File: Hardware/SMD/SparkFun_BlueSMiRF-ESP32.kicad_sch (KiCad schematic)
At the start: 27 parts, among them J1 Conn_01x06, Q1 Q_NMOS_DGS, Q2 Q_NMOS_DGS, SW1 Switch, U1 ESP32_Pico_Mini, U2 AP2112K-3.3

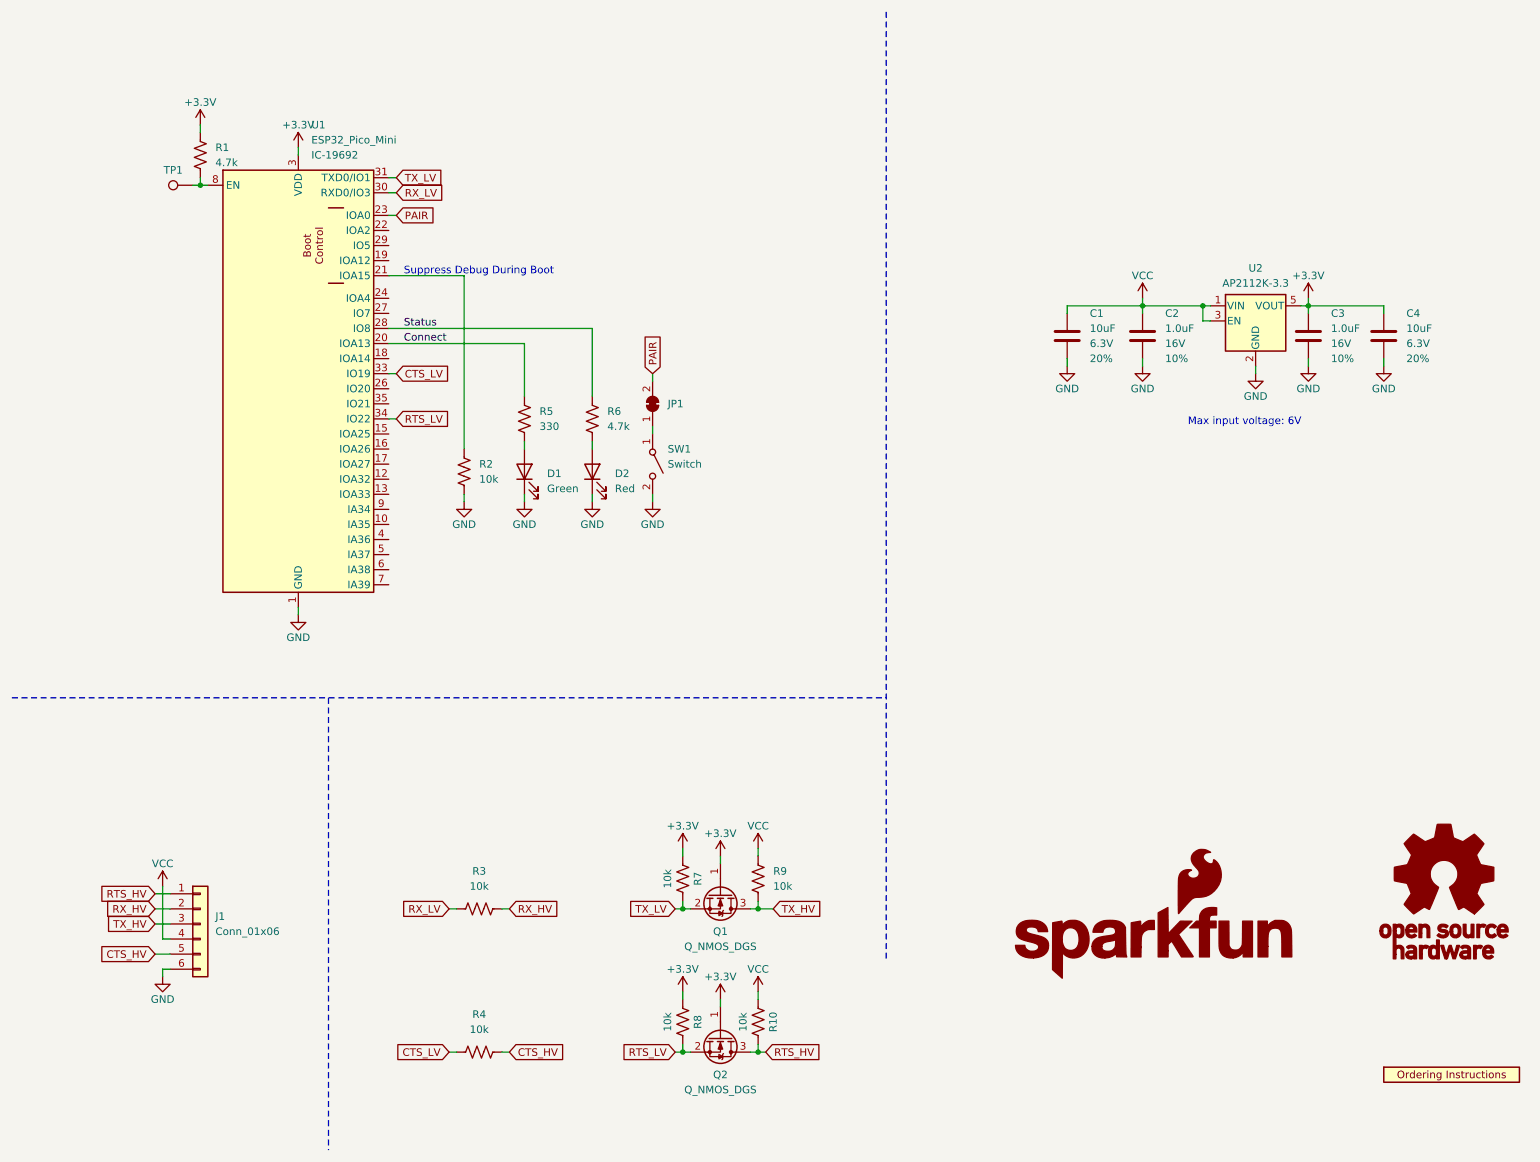
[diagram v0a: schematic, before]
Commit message: Post design review fixes.
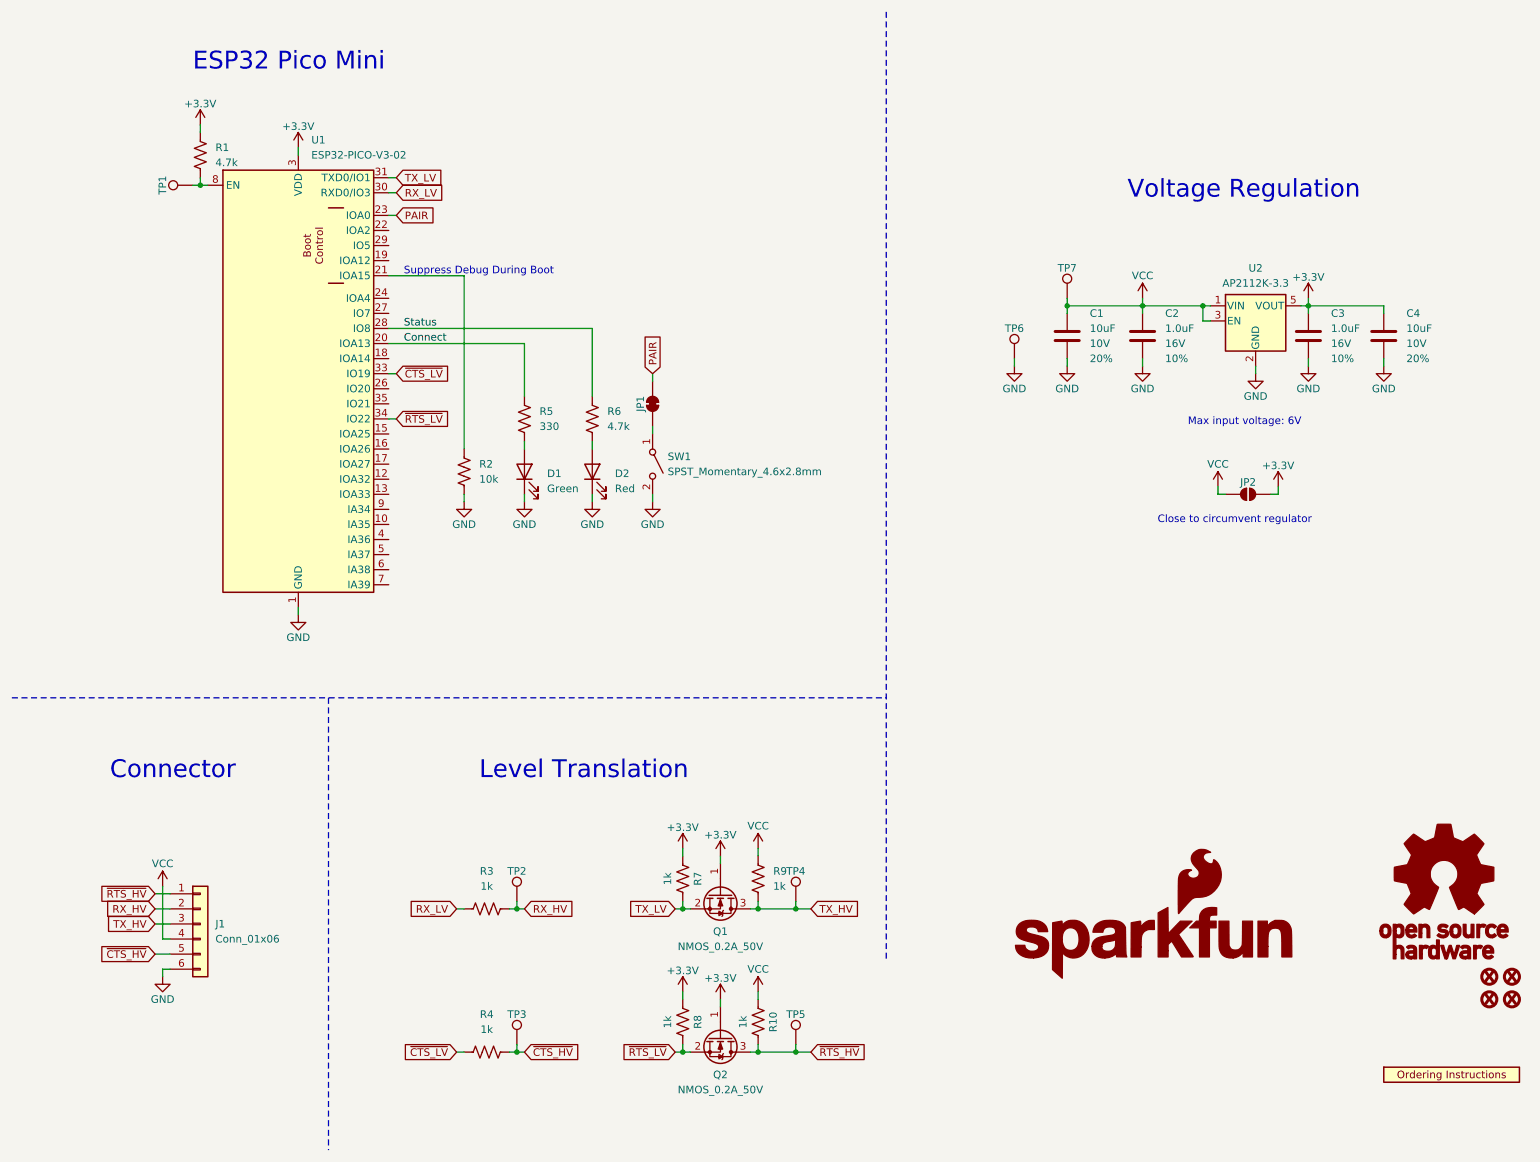
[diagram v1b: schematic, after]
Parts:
- added FID1, FID2, FID3, FID4: Fiducial_0.5, SparkFun-Aesthetic:Fiducial_0.5mm_Mask1mm, symbol SparkFun-Aesthetic:Fiducial_0.5
- added JP2: ~, SparkFun-Jumper:SMT-JUMPER_2_NO_SILK, symbol SparkFun-Jumper:SolderJumper_2_Open
- added TP2, TP3, TP4, TP5, TP6, TP7: TestPoint_0.75mm, SparkFun-Connector:TestPoint-0.75mm, symbol SparkFun-Connector:TestPoint_0.75mm
- C1, C4: symbol SparkFun-Capacitor:10uF_0603_6.3V_20% -> SparkFun-Capacitor:10uF_0603_10V_20%; PROD_ID CAP-11015 -> CAP-20155; Voltage 6.3V -> 10V
- Q1, Q2: value Q_NMOS_DGS -> NMOS_0.2A_50V
- R10, R3, R4, R7, R8, R9: value 10k -> 1k; symbol SparkFun-Resistor:10k_0603 -> SparkFun-Resistor:1k_0603; PROD_ID RES-00824 -> RES-07856
- SW1: value Switch -> SPST_Momentary_4.6x2.8mm
- U1: value ESP32_Pico_Mini -> ESP32-PICO-V3-02
- U3: footprint SparkFun-Aesthetic:Ordering_Instructions -> SparkFun-Aesthetic:ORDERING_INSTRUCTIONS
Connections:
- net +3.3V: now also JP2.2 (B)
- net GND: now also TP6.1
- net RX_HV: now also TP2.1
- net TX_HV: now also TP4.1
- net VCC: now also JP2.1 (A), TP7.1
- net CTS_HV renamed ~{CTS_HV}
- net ~{CTS_HV}: now also TP3.1
- net CTS_LV renamed ~{CTS_LV}
- net RTS_HV renamed ~{RTS_HV}
- net ~{RTS_HV}: now also TP5.1
- net RTS_LV renamed ~{RTS_LV}
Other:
- note added: "Close to circumvent regulator"
- note added: "Connector"
- note added: "ESP32 Pico Mini"
- note added: "Level Translation"
- note added: "Voltage Regulation"
- title: BlueSMiRF - ESP32 -> SparkFun BlueSMiRF - ESP32
- moved on the sheet: R3, R4

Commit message: Change BSS138 resistors to 10k
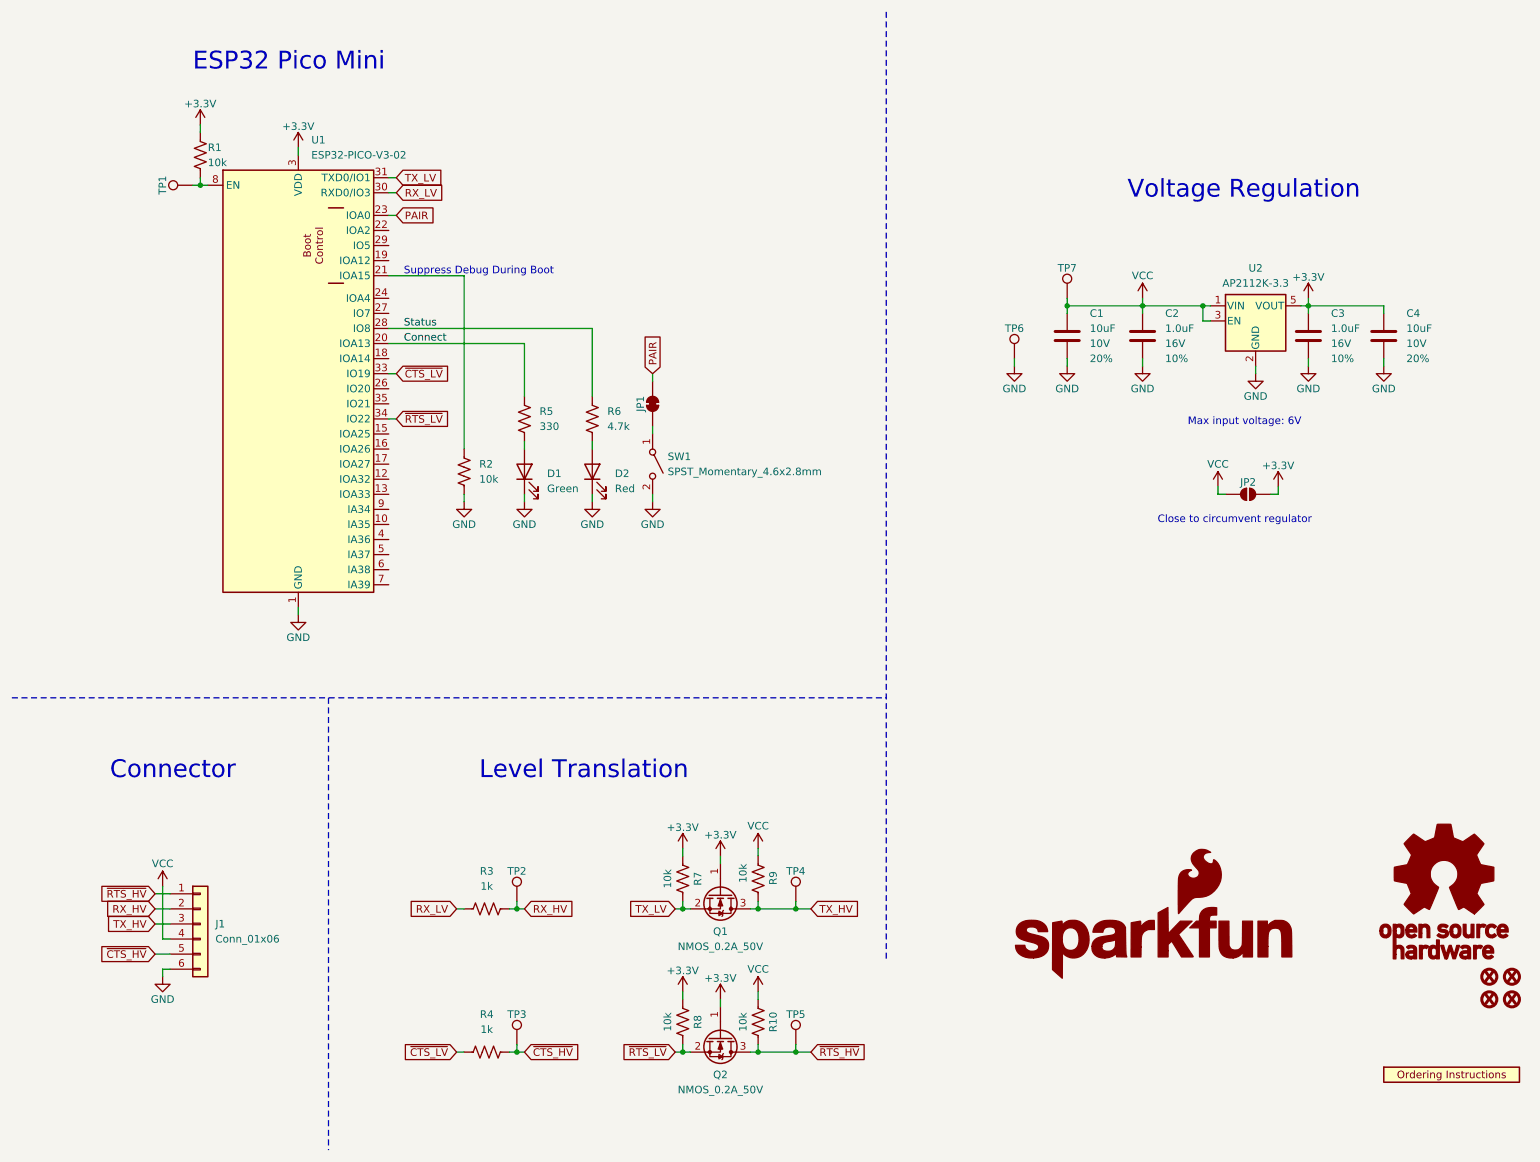
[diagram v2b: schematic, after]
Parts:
- R1: value 4.7k -> 10k; symbol SparkFun-Resistor:4.7k_0603 -> SparkFun-Resistor:10k_0603; PROD_ID RES-07857 -> RES-00824
- R10, R7, R8, R9: value 1k -> 10k; symbol SparkFun-Resistor:1k_0603 -> SparkFun-Resistor:10k_0603; PROD_ID RES-07856 -> RES-00824
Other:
- moved on the sheet: R1, R10, R7, R8, R9
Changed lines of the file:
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@@
     )
   )
-  (symbol (lib_id "SparkFun-Resistor:1k_0603") (at 125.73 157.48 0) (unit 1)
-    (in_bom yes) (on_board yes) (dnp no)
-    (property "Reference" "R7" (at 128.27 157.48 90)
-      (effects (font (size 1.27 1.27)))
-    )
-    (property "Value" "1k" (at 123.19 157.48 90)
-      (effects (font (size 1.27 1.27)))
-    )
-    (property "Footprint" "SparkFun-Resistor:R_0603_1608Metric" (at 130.302 157.48 90)
-      (effects (font (size 1.27 1.27)) hide)
-    )
-    (property "Datasheet" "https://www.vishay.com/docs/20035/dcrcwe3.pdf" (at 134.62 158.75 90)
-      (effects (font (size 1.27 1.27)) hide)
-    )
-    (property "PROD_ID" "RES-07856" (at 132.588 157.48 90)
+  (symbol (lib_name "10k_0603_1") (lib_id "SparkFun-Resistor:10k_0603") (at 125.73 157.48 90) (unit 1)
+    (in_bom yes) (on_board yes) (dnp no)
+    (property "Reference" "R7" (at 128.27 157.48 0)
+      (effects (font (size 1.27 1.27)))
+    )
+    (property "Value" "10k" (at 123.19 157.48 0)
+      (effects (font (size 1.27 1.27)))
+    )
+    (property "Footprint" "SparkFun-Resistor:R_0603_1608Metric" (at 130.048 157.48 0)
+      (effects (font (size 1.27 1.27)) hide)
+    )
+    (property "Datasheet" "https://www.vishay.com/docs/20035/dcrcwe3.pdf" (at 133.35 157.48 0)
+      (effects (font (size 1.27 1.27)) hide)
+    )
+    (property "PROD_ID" "RES-00824" (at 132.08 157.48 0)
       (effects (font (size 1.27 1.27)) hide)
     )
@@
     )
   )
-  (symbol (lib_id "SparkFun-Resistor:1k_0603") (at 138.43 157.48 0) (unit 1)
-    (in_bom yes) (on_board yes) (dnp no) (fields_autoplaced)
+  (symbol (lib_name "10k_0603_2") (lib_id "SparkFun-Resistor:10k_0603") (at 138.43 157.48 90) (unit 1)
+    (in_bom yes) (on_board yes) (dnp no)
     (property "Reference" "R9" (at 140.97 156.21 0)
-      (effects (font (size 1.27 1.27)) (justify left))
-    )
-    (property "Value" "1k" (at 140.97 158.75 0)
-      (effects (font (size 1.27 1.27)) (justify left))
-    )
-    (property "Footprint" "SparkFun-Resistor:R_0603_1608Metric" (at 143.002 157.48 90)
-      (effects (font (size 1.27 1.27)) hide)
-    )
-    (property "Datasheet" "https://www.vishay.com/docs/20035/dcrcwe3.pdf" (at 147.32 158.75 90)
-      (effects (font (size 1.27 1.27)) hide)
-    )
-    (property "PROD_ID" "RES-07856" (at 145.288 157.48 90)
+      (effects (font (size 1.27 1.27)) (justify right))
+    )
+    (property "Value" "10k" (at 135.89 154.94 0)
+      (effects (font (size 1.27 1.27)) (justify right))
+    )
+    (property "Footprint" "SparkFun-Resistor:R_0603_1608Metric" (at 142.748 157.48 0)
+      (effects (font (size 1.27 1.27)) hide)
+    )
+    (property "Datasheet" "https://www.vishay.com/docs/20035/dcrcwe3.pdf" (at 146.05 157.48 0)
+      (effects (font (size 1.27 1.27)) hide)
+    )
+    (property "PROD_ID" "RES-00824" (at 144.78 157.48 0)
       (effects (font (size 1.27 1.27)) hide)
     )
@@
     )
   )
-  (symbol (lib_id "SparkFun-Resistor:1k_0603") (at 125.73 181.61 0) (unit 1)
-    (in_bom yes) (on_board yes) (dnp no)
-    (property "Reference" "R8" (at 128.27 181.61 90)
-      (effects (font (size 1.27 1.27)))
-    )
-    (property "Value" "1k" (at 123.19 181.61 90)
-      (effects (font (size 1.27 1.27)))
-    )
-    (property "Footprint" "SparkFun-Resistor:R_0603_1608Metric" (at 130.302 181.61 90)
-      (effects (font (size 1.27 1.27)) hide)
-    )
-    (property "Datasheet" "https://www.vishay.com/docs/20035/dcrcwe3.pdf" (at 134.62 182.88 90)
-      (effects (font (size 1.27 1.27)) hide)
-    )
-    (property "PROD_ID" "RES-07856" (at 132.588 181.61 90)
+  (symbol (lib_name "10k_0603_3") (lib_id "SparkFun-Resistor:10k_0603") (at 125.73 181.61 90) (unit 1)
+    (in_bom yes) (on_board yes) (dnp no)
+    (property "Reference" "R8" (at 128.27 181.61 0)
+      (effects (font (size 1.27 1.27)))
+    )
+    (property "Value" "10k" (at 123.19 181.61 0)
+      (effects (font (size 1.27 1.27)))
+    )
+    (property "Footprint" "SparkFun-Resistor:R_0603_1608Metric" (at 130.048 181.61 0)
+      (effects (font (size 1.27 1.27)) hide)
+    )
+    (property "Datasheet" "https://www.vishay.com/docs/20035/dcrcwe3.pdf" (at 133.35 181.61 0)
+      (effects (font (size 1.27 1.27)) hide)
+    )
+    (property "PROD_ID" "RES-00824" (at 132.08 181.61 0)
       (effects (font (size 1.27 1.27)) hide)
     )
@@
     )
   )
-  (symbol (lib_id "SparkFun-Resistor:1k_0603") (at 138.43 181.61 0) (unit 1)
-    (in_bom yes) (on_board yes) (dnp no)
-    (property "Reference" "R10" (at 140.97 181.61 90)
-      (effects (font (size 1.27 1.27)))
-    )
-    (property "Value" "1k" (at 135.89 181.61 90)
-      (effects (font (size 1.27 1.27)))
-    )
-    (property "Footprint" "SparkFun-Resistor:R_0603_1608Metric" (at 143.002 181.61 90)
-      (effects (font (size 1.27 1.27)) hide)
-    )
-    (property "Datasheet" "https://www.vishay.com/docs/20035/dcrcwe3.pdf" (at 147.32 182.88 90)
-      (effects (font (size 1.27 1.27)) hide)
-    )
-    (property "PROD_ID" "RES-07856" (at 145.288 181.61 90)
+  (symbol (lib_name "10k_0603_5") (lib_id "SparkFun-Resistor:10k_0603") (at 138.43 181.61 90) (unit 1)
+    (in_bom yes) (on_board yes) (dnp no)
+    (property "Reference" "R10" (at 140.97 181.61 0)
+      (effects (font (size 1.27 1.27)))
+    )
+    (property "Value" "10k" (at 135.89 181.61 0)
+      (effects (font (size 1.27 1.27)))
+    )
+    (property "Footprint" "SparkFun-Resistor:R_0603_1608Metric" (at 142.748 181.61 0)
+      (effects (font (size 1.27 1.27)) hide)
+    )
+    (property "Datasheet" "https://www.vishay.com/docs/20035/dcrcwe3.pdf" (at 146.05 181.61 0)
+      (effects (font (size 1.27 1.27)) hide)
+    )
+    (property "PROD_ID" "RES-00824" (at 144.78 181.61 0)
       (effects (font (size 1.27 1.27)) hide)
     )
@@
     )
   )
-  (symbol (lib_id "SparkFun-Resistor:4.7k_0603") (at 44.45 35.56 0) (unit 1)
-    (in_bom yes) (on_board yes) (dnp no) (fields_autoplaced)
-    (property "Reference" "R1" (at 46.99 34.29 0)
-      (effects (font (size 1.27 1.27)) (justify left))
-    )
-    (property "Value" "4.7k" (at 46.99 36.83 0)
-      (effects (font (size 1.27 1.27)) (justify left))
-    )
-    (property "Footprint" "SparkFun-Resistor:R_0603_1608Metric" (at 48.768 35.56 90)
-      (effects (font (size 1.27 1.27)) hide)
-    )
-    (property "Datasheet" "https://www.vishay.com/docs/20035/dcrcwe3.pdf" (at 53.34 35.56 90)
-      (effects (font (size 1.27 1.27)) hide)
-    )
-    (property "PROD_ID" "RES-07857" (at 51.054 35.56 90)
-      (effects (font (size 1.27 1.27)) hide)
-    )
+  (symbol (lib_name "10k_0603_4") (lib_id "SparkFun-Resistor:10k_0603") (at 44.45 35.56 90) (unit 1)
+    (in_bom yes) (on_board yes) (dnp no)
+    (property "Reference" "R1" (at 45.72 34.29 90)
+      (effects (font (size 1.27 1.27)) (justify right))
+    )
+    (property "Value" "10k" (at 45.72 36.83 90)
+      (effects (font (size 1.27 1.27)) (justify right))
+    )
+    (property "Footprint" "SparkFun-Resistor:R_0603_1608Metric" (at 48.768 35.56 0)
+      (effects (font (size 1.27 1.27)) hide)
+    )
+    (property "Datasheet" "https://www.vishay.com/docs/20035/dcrcwe3.pdf" (at 52.07 35.56 0)
+      (effects (font (size 1.27 1.27)) hide)
+    )
+    (property "PROD_ID" "RES-00824" (at 50.8 35.56 0)
+      (effects (font (size 1.27 1.27)) hide)
+    )
